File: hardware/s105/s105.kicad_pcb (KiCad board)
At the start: 2 copper layers, 20 parts, among them Q1 BC847C

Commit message: разместила схожие блоки
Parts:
- added C10: 2.2uF, Capacitor_SMD:C_0603_1608Metric, F.Cu at (219.5, 145.0)
- added C11: 2.2uF, Capacitor_SMD:C_0603_1608Metric, F.Cu at (228.2, 128.6)
- added C12: 1uF, Capacitor_SMD:C_0603_1608Metric, F.Cu at (208.7, 143.7)
- added C13: 10nF, Capacitor_SMD:C_0603_1608Metric, F.Cu at (269.1, 115.5)
- added C14: 100nF, Capacitor_SMD:C_0603_1608Metric, F.Cu at (221.0, 144.5)
- added C15: 100nF, Capacitor_SMD:C_0603_1608Metric, F.Cu at (225.8, 125.0)
- added C16: 100nF, Capacitor_SMD:C_0603_1608Metric, F.Cu at (203.9, 130.8)
- added C17: 100nF, Capacitor_SMD:C_0603_1608Metric, F.Cu at (208.9, 121.9)
- added C18: 100nF, Capacitor_SMD:C_0603_1608Metric, F.Cu at (208.7, 120.3)
- added C25: C0603, Capacitor_SMD:C_0603_1608Metric, F.Cu at (77.4, 181.7)
- added C26: C0603, Capacitor_SMD:C_0603_1608Metric, F.Cu at (77.4, 183.2)
- added C27: C0603, Capacitor_SMD:C_0603_1608Metric, F.Cu at (77.4, 178.7)
- added C28: NM, Capacitor_SMD:C_0603_1608Metric, F.Cu at (77.4, 180.2)
- added C29: C0603, Capacitor_SMD:C_0603_1608Metric, F.Cu at (77.4, 177.2)
- added C30: C0603, Capacitor_SMD:C_0603_1608Metric, F.Cu at (77.4, 175.7)
- added C31: C0603, Capacitor_SMD:C_0603_1608Metric, F.Cu at (77.4, 174.2)
- added C32: C0603, Capacitor_SMD:C_0603_1608Metric, F.Cu at (77.5, 187.4)
- added C33: C0603, Capacitor_SMD:C_0603_1608Metric, F.Cu at (77.5, 192.0)
- added C34: C0603, Capacitor_SMD:C_0603_1608Metric, F.Cu at (77.4, 207.0)
- added C35: C0603, Capacitor_SMD:C_0603_1608Metric, F.Cu at (77.5, 190.5)
- added C36: C0603, Capacitor_SMD:C_0603_1608Metric, F.Cu at (77.5, 188.9)
- added C37: C0603, Capacitor_SMD:C_0603_1608Metric, F.Cu at (77.4, 201.8)
- added C38: C0603, Capacitor_SMD:C_0603_1608Metric, F.Cu at (77.3, 205.1)
- added C39: C0603, Capacitor_SMD:C_0603_1608Metric, F.Cu at (77.3, 203.5)
- added C4: C0603, Capacitor_SMD:C_0603_1608Metric, F.Cu at (77.5, 184.7)
- added C40: C0603, Capacitor_SMD:C_0603_1608Metric, F.Cu at (77.5, 193.5)
- added C41: ~, Capacitor_SMD:C_0603_1608Metric, F.Cu at (99.4, 103.8)
- added C42: ~, Capacitor_SMD:C_0603_1608Metric, F.Cu at (101.3, 105.4)
- added C43: C_Small, Capacitor_SMD:C_1206_3216Metric, F.Cu at (74.9, 114.2)
- added C44: ~, Capacitor_SMD:C_0603_1608Metric, F.Cu at (142.7, 127.9)
- added C45: ~, Capacitor_SMD:C_0603_1608Metric, F.Cu at (142.9, 122.8)
- added C46: C_Small, Capacitor_SMD:C_1206_3216Metric, F.Cu at (77.8, 117.4)
- added C47: ~, Capacitor_SMD:C_0603_1608Metric, F.Cu at (139.1, 98.9)
- added C48: ~, Capacitor_SMD:C_0603_1608Metric, F.Cu at (142.4, 94.7)
- added C49: C_Small, Capacitor_SMD:C_1206_3216Metric, F.Cu at (73.9, 100.6)
- added C5: 10nF, Capacitor_SMD:C_0603_1608Metric, F.Cu at (264.8, 113.0)
- added C50: C0603, Capacitor_SMD:C_0603_1608Metric, F.Cu at (134.4, 236.0)
- added C51: C0805, Capacitor_SMD:C_0805_2012Metric, F.Cu at (196.2, 152.1)
- added C52: 100nF, Capacitor_SMD:C_0603_1608Metric, F.Cu at (200.4, 138.8)
- added C53: 100nF, Capacitor_SMD:C_0603_1608Metric, F.Cu at (197.4, 137.2)
- added C6: 18pF, Capacitor_SMD:C_0603_1608Metric, F.Cu at (199.3, 128.1)
- added C7: 18pF, Capacitor_SMD:C_0603_1608Metric, F.Cu at (199.3, 131.0)
- added C8: 1uF, Capacitor_SMD:C_0603_1608Metric, F.Cu at (200.0, 136.3)
- added C9: 100nF, Capacitor_SMD:C_0603_1608Metric, F.Cu at (227.8, 125.5)
- added D10: 1N4148W, Diode_SMD:D_SOD-123, F.Cu at (148.4, 98.5)
- added D11: BYG2OG, Diode_SMD:D_SMA, F.Cu at (151.9, 299.9)
- added D12: BYG2OG, Diode_SMD:D_SMA, F.Cu at (58.2, 297.1)
- added D13: BYG2OG, Diode_SMD:D_SMA, F.Cu at (216.6, 220.0)
- added D14: BYG2OG, Diode_SMD:D_SMA, F.Cu at (136.8, 260.6)
- added D15: 1N4148W, Diode_SMD:D_SOD-123, F.Cu at (125.7, 242.6)
- added D16: BYG2OG, Diode_SMD:D_SMA, F.Cu at (155.0, 237.6)
- added D17: BYG2OG, Diode_SMD:D_SMA, F.Cu at (108.3, 287.8)
- added D18: BYG2OG, Diode_SMD:D_SMA, F.Cu at (78.7, 269.3)
- added D19: BYG2OG, Diode_SMD:D_SMA, F.Cu at (208.0, 305.7)
- added D20: BYG2OG, Diode_SMD:D_SMA, F.Cu at (192.1, 199.4)
- added D7: BYG2OG, Diode_SMD:D_SMA, F.Cu at (123.2, 201.6)
- added D8: 1N4148W, Diode_SMD:D_SOD-123, F.Cu at (91.0, 103.9)
- added D9: 1N4148W, Diode_SMD:D_SOD-123, F.Cu at (147.6, 124.3)
- added J1: Conn_01x06, Connector_JST:JST_EH_B6B-EH-A_1x06_P2.50mm_Vertical, F.Cu at (230.6, 142.8)
- added P1: 368255-2, hellen121vag:368255-2, F.Cu at (126.1, 113.7)
- added Q10: BC847C, Package_TO_SOT_SMD:SOT-23, F.Cu at (220.9, 168.0)
- added Q11: BC847C, Package_TO_SOT_SMD:SOT-23, F.Cu at (127.3, 189.4)
- added Q12: BC847C, Package_TO_SOT_SMD:SOT-23, F.Cu at (156.0, 271.3)
- added Q13: BC847C, Package_TO_SOT_SMD:SOT-23, F.Cu at (176.3, 297.4)
- added Q14: BC847C, Package_TO_SOT_SMD:SOT-23, F.Cu at (81.3, 298.0)
- added Q15: BC847C, Package_TO_SOT_SMD:SOT-23, F.Cu at (220.2, 196.9)
- added Q16: BC847C, Package_TO_SOT_SMD:SOT-23, F.Cu at (118.0, 240.3)
- added Q17: ., Package_TO_SOT_SMD:SOT-23, F.Cu at (127.7, 236.6)
- added Q18: BC847C, Package_TO_SOT_SMD:SOT-23, F.Cu at (180.7, 226.6)
- added Q19: ., Package_TO_SOT_SMD:SOT-23, F.Cu at (118.0, 236.8)
- added Q2: BC847C, Package_TO_SOT_SMD:SOT-23, F.Cu at (146.4, 209.7)
- added Q20: BC847C, Package_TO_SOT_SMD:SOT-23, F.Cu at (130.3, 296.8)
- added Q21: BC847C, Package_TO_SOT_SMD:SOT-23, F.Cu at (103.6, 264.6)
- added Q22: BC847C, Package_TO_SOT_SMD:SOT-23, F.Cu at (219.6, 284.9)
- added Q23: BC847C, Package_TO_SOT_SMD:SOT-23, F.Cu at (177.6, 216.8)
- added Q24: ., Package_TO_SOT_SMD:SOT-23, F.Cu at (217.8, 150.6)
- added Q25: ., Package_TO_SOT_SMD:SOT-23, F.Cu at (214.1, 150.7)
- added Q26: ., Package_TO_SOT_SMD:SOT-23, F.Cu at (210.4, 150.6)
- added Q27: ., Package_TO_SOT_SMD:SOT-23, F.Cu at (221.3, 150.6)
- added Q28: ., Package_TO_SOT_SMD:SOT-23, F.Cu at (195.3, 148.3)
- added Q29: ., Package_TO_SOT_SMD:SOT-23, F.Cu at (201.1, 119.1)
- added Q3: BC847C, Package_TO_SOT_SMD:SOT-23, F.Cu at (92.0, 211.5)
- added Q30: ., Package_TO_SOT_SMD:SOT-23, F.Cu at (198.6, 123.1)
- added Q31: ., Package_TO_SOT_SMD:SOT-23, F.Cu at (214.0, 115.4)
- added Q32: ., Package_TO_SOT_SMD:SOT-23, F.Cu at (216.6, 109.3)
- added Q33: ., Package_TO_SOT_SMD:SOT-23, F.Cu at (221.0, 118.8)
- added Q4: BC847C, Package_TO_SOT_SMD:SOT-23, F.Cu at (210.5, 260.0)
- added Q5: ., Package_TO_SOT_SMD:SOT-23, F.Cu at (216.4, 253.8)
- added Q6: ., Package_TO_SOT_SMD:SOT-23, F.Cu at (221.6, 252.6)
- added Q7: BC847C, Package_TO_SOT_SMD:SOT-23, F.Cu at (105.8, 224.8)
- added Q8: BC847C, Package_TO_SOT_SMD:SOT-23, F.Cu at (201.7, 225.9)
- added Q9: BC847C, Package_TO_SOT_SMD:SOT-23, F.Cu at (193.6, 177.4)
- added R100: 1R, Resistor_SMD:R_1206_3216Metric, F.Cu at (210.2, 173.9)
- added R101: 1R, Resistor_SMD:R_1206_3216Metric, F.Cu at (210.2, 177.7)
- added R102: 82K, Resistor_SMD:R_0805_2012Metric, F.Cu at (211.1, 188.5)
- added R103: 51K, Resistor_SMD:R_0603_1608Metric, F.Cu at (207.7, 187.4)
- added R104: 3K, Resistor_SMD:R_0603_1608Metric, F.Cu at (128.0, 182.7)
- added R105: 3K, Resistor_SMD:R_0603_1608Metric, F.Cu at (128.1, 185.2)
- added R106: 360R, Resistor_SMD:R_0603_1608Metric, F.Cu at (128.5, 194.6)
- added R107: 1R, Resistor_SMD:R_1206_3216Metric, F.Cu at (139.2, 196.2)
- added R108: 1R, Resistor_SMD:R_1206_3216Metric, F.Cu at (132.5, 196.3)
- added R109: 1R, Resistor_SMD:R_1206_3216Metric, F.Cu at (135.9, 196.2)
- added R110: 82K, Resistor_SMD:R_0805_2012Metric, F.Cu at (145.6, 195.6)
- added R111: 51K, Resistor_SMD:R_0603_1608Metric, F.Cu at (144.7, 198.5)
- added R112: 3K, Resistor_SMD:R_0603_1608Metric, F.Cu at (155.2, 267.5)
- added R113: 3K, Resistor_SMD:R_0603_1608Metric, F.Cu at (160.1, 270.2)
- added R114: 360R, Resistor_SMD:R_0603_1608Metric, F.Cu at (157.5, 278.6)
- added R115: 1R, Resistor_SMD:R_1206_3216Metric, F.Cu at (168.2, 280.4)
- added R116: 1R, Resistor_SMD:R_1206_3216Metric, F.Cu at (161.0, 280.1)
- added R117: 1R, Resistor_SMD:R_1206_3216Metric, F.Cu at (164.6, 280.3)
- added R118: 82K, Resistor_SMD:R_0805_2012Metric, F.Cu at (173.2, 278.8)
- added R119: 51K, Resistor_SMD:R_0603_1608Metric, F.Cu at (172.3, 281.7)
- added R120: 3K, Resistor_SMD:R_0603_1608Metric, F.Cu at (177.2, 301.4)
- added R121: 3K, Resistor_SMD:R_0603_1608Metric, F.Cu at (171.8, 298.7)
- added R122: 360R, Resistor_SMD:R_0603_1608Metric, F.Cu at (176.0, 290.8)
- added R123: 1R, Resistor_SMD:R_1206_3216Metric, F.Cu at (163.9, 290.0)
- added R124: 1R, Resistor_SMD:R_1206_3216Metric, F.Cu at (171.2, 290.2)
- added R125: 1R, Resistor_SMD:R_1206_3216Metric, F.Cu at (167.6, 290.0)
- added R126: 82K, Resistor_SMD:R_0805_2012Metric, F.Cu at (158.7, 290.8)
- added R127: 51K, Resistor_SMD:R_0603_1608Metric, F.Cu at (159.5, 287.6)
- added R128: 3K, Resistor_SMD:R_0603_1608Metric, F.Cu at (82.0, 302.1)
- added R129: 3K, Resistor_SMD:R_0603_1608Metric, F.Cu at (76.7, 299.6)
- added R130: 360R, Resistor_SMD:R_0603_1608Metric, F.Cu at (80.5, 290.8)
- added R131: 1R, Resistor_SMD:R_1206_3216Metric, F.Cu at (68.1, 290.4)
- added R132: 1R, Resistor_SMD:R_1206_3216Metric, F.Cu at (74.9, 290.3)
- added R133: 1R, Resistor_SMD:R_1206_3216Metric, F.Cu at (71.4, 290.3)
- added R134: 82K, Resistor_SMD:R_0805_2012Metric, F.Cu at (63.6, 291.5)
- added R135: 51K, Resistor_SMD:R_0603_1608Metric, F.Cu at (64.5, 288.4)
- added R136: 3K, Resistor_SMD:R_0603_1608Metric, F.Cu at (224.2, 196.6)
- added R137: 3K, Resistor_SMD:R_0603_1608Metric, F.Cu at (221.0, 201.6)
- added R138: 360R, Resistor_SMD:R_0603_1608Metric, F.Cu at (215.0, 196.4)
- added R139: 1R, Resistor_SMD:R_1206_3216Metric, F.Cu at (211.3, 207.9)
- added R14: 10K, Resistor_SMD:R_0603_1608Metric, F.Cu at (268.8, 111.5)
- added R140: 1R, Resistor_SMD:R_1206_3216Metric, F.Cu at (211.8, 201.7)
- added R141: 1R, Resistor_SMD:R_1206_3216Metric, F.Cu at (211.4, 204.6)
- added R142: 82K, Resistor_SMD:R_0805_2012Metric, F.Cu at (212.3, 214.3)
- added R143: 51K, Resistor_SMD:R_0603_1608Metric, F.Cu at (208.7, 215.2)
- added R144: 3K, Resistor_SMD:R_0603_1608Metric, F.Cu at (119.1, 245.3)
- added R145: 3K, Resistor_SMD:R_0603_1608Metric, F.Cu at (121.4, 245.1)
- added R146: 360R, Resistor_SMD:R_0603_1608Metric, F.Cu at (113.7, 255.3)
- added R147: 1R, Resistor_SMD:R_1206_3216Metric, F.Cu at (124.4, 260.1)
- added R148: 1R, Resistor_SMD:R_1206_3216Metric, F.Cu at (117.8, 260.0)
- added R149: 1R, Resistor_SMD:R_1206_3216Metric, F.Cu at (121.3, 260.1)
- added R15: 10K, Resistor_SMD:R_0603_1608Metric, F.Cu at (265.1, 115.5)
- added R150: 82K, Resistor_SMD:R_0805_2012Metric, F.Cu at (139.5, 253.6)
- added R151: 51K, Resistor_SMD:R_0603_1608Metric, F.Cu at (139.5, 251.2)
- added R152: 6.8k, Resistor_SMD:R_0603_1608Metric, F.Cu at (134.4, 233.8)
- added R153: 100, Resistor_SMD:R_0603_1608Metric, F.Cu at (130.6, 233.8)
- added R154: 68k, Resistor_SMD:R_0603_1608Metric, F.Cu at (131.9, 236.8)
- added R155: 4.7k, Resistor_SMD:R_1206_3216Metric, F.Cu at (133.4, 239.9)
- added R156: 4.7k, Resistor_SMD:R_1206_3216Metric, F.Cu at (133.4, 242.3)
- added R157: 10k, Resistor_SMD:R_0805_2012Metric, F.Cu at (128.7, 241.9)
- added R158: 100, Resistor_SMD:R_0603_1608Metric, F.Cu at (121.5, 235.9)
- added R159: 3K, Resistor_SMD:R_0603_1608Metric, F.Cu at (176.3, 234.9)
- added R160: 3K, Resistor_SMD:R_0603_1608Metric, F.Cu at (179.6, 235.9)
- added R161: 360R, Resistor_SMD:R_0603_1608Metric, F.Cu at (181.1, 224.0)
- added R162: 1R, Resistor_SMD:R_1206_3216Metric, F.Cu at (173.9, 222.4)
- added R163: 1R, Resistor_SMD:R_1206_3216Metric, F.Cu at (174.0, 227.0)
- added R164: 1R, Resistor_SMD:R_1206_3216Metric, F.Cu at (174.0, 224.7)
- added R165: 82K, Resistor_SMD:R_0805_2012Metric, F.Cu at (161.6, 227.1)
- added R166: 51K, Resistor_SMD:R_0603_1608Metric, F.Cu at (162.3, 223.6)
- added R167: 3K, Resistor_SMD:R_0603_1608Metric, F.Cu at (131.0, 300.5)
- added R168: 3K, Resistor_SMD:R_0603_1608Metric, F.Cu at (126.2, 298.0)
- added R169: 360R, Resistor_SMD:R_0603_1608Metric, F.Cu at (129.5, 291.4)
- added R170: 1R, Resistor_SMD:R_1206_3216Metric, F.Cu at (118.3, 289.3)
- added R171: 1R, Resistor_SMD:R_1206_3216Metric, F.Cu at (125.4, 289.4)
- added R172: 1R, Resistor_SMD:R_1206_3216Metric, F.Cu at (121.7, 289.3)
- added R173: 82K, Resistor_SMD:R_0805_2012Metric, F.Cu at (113.2, 290.1)
- added R174: 51K, Resistor_SMD:R_0603_1608Metric, F.Cu at (114.1, 286.6)
- added R175: 3K, Resistor_SMD:R_0603_1608Metric, F.Cu at (104.0, 268.5)
- added R176: 3K, Resistor_SMD:R_0603_1608Metric, F.Cu at (99.8, 266.3)
- added R177: 360R, Resistor_SMD:R_0603_1608Metric, F.Cu at (103.5, 258.8)
- added R178: 1R, Resistor_SMD:R_1206_3216Metric, F.Cu at (92.6, 257.2)
- added R179: 1R, Resistor_SMD:R_1206_3216Metric, F.Cu at (99.0, 257.0)
- added R180: 1R, Resistor_SMD:R_1206_3216Metric, F.Cu at (95.8, 257.2)
- added R181: 82K, Resistor_SMD:R_0805_2012Metric, F.Cu at (86.6, 257.2)
- added R182: 51K, Resistor_SMD:R_0603_1608Metric, F.Cu at (87.5, 254.1)
- added R183: 3K, Resistor_SMD:R_0603_1608Metric, F.Cu at (225.4, 284.9)
- added R184: 3K, Resistor_SMD:R_0603_1608Metric, F.Cu at (225.4, 289.3)
- added R185: 360R, Resistor_SMD:R_0603_1608Metric, F.Cu at (214.9, 281.0)
- added R186: 1R, Resistor_SMD:R_1206_3216Metric, F.Cu at (209.7, 296.3)
- added R187: 1R, Resistor_SMD:R_1206_3216Metric, F.Cu at (209.9, 289.1)
- added R188: 1R, Resistor_SMD:R_1206_3216Metric, F.Cu at (209.9, 292.6)
- added R189: 82K, Resistor_SMD:R_0805_2012Metric, F.Cu at (210.2, 300.8)
- added R19: 3K, Resistor_SMD:R_0603_1608Metric, F.Cu at (147.2, 213.6)
- added R190: 51K, Resistor_SMD:R_0603_1608Metric, F.Cu at (206.7, 299.9)
- added R191: 3K, Resistor_SMD:R_0603_1608Metric, F.Cu at (175.2, 205.1)
- added R192: 3K, Resistor_SMD:R_0603_1608Metric, F.Cu at (180.1, 207.7)
- added R193: 360R, Resistor_SMD:R_0603_1608Metric, F.Cu at (179.1, 213.6)
- added R194: 1R, Resistor_SMD:R_1206_3216Metric, F.Cu at (190.3, 217.2)
- added R195: 1R, Resistor_SMD:R_1206_3216Metric, F.Cu at (182.6, 216.8)
- added R196: 1R, Resistor_SMD:R_1206_3216Metric, F.Cu at (186.8, 217.0)
- added R197: 82K, Resistor_SMD:R_0805_2012Metric, F.Cu at (193.8, 216.2)
- added R198: 51K, Resistor_SMD:R_0603_1608Metric, F.Cu at (192.8, 219.3)
- added R199: 6.8k, Resistor_SMD:R_0603_1608Metric, F.Cu at (198.9, 152.0)
- added R20: 3K, Resistor_SMD:R_0603_1608Metric, F.Cu at (142.3, 210.8)
- added R200: 68k, Resistor_SMD:R_0603_1608Metric, F.Cu at (200.9, 151.9)
- added R201: R0603, Resistor_SMD:R_0603_1608Metric, F.Cu at (194.4, 133.6)
- added R202: 300, Resistor_SMD:R_0603_1608Metric, F.Cu at (201.0, 131.0)
- added R21: 360R, Resistor_SMD:R_0603_1608Metric, F.Cu at (144.3, 204.2)
- added R22: 1R, Resistor_SMD:R_1206_3216Metric, F.Cu at (133.5, 202.1)
- added R23: 1R, Resistor_SMD:R_1206_3216Metric, F.Cu at (140.5, 202.1)
- added R24: 1R, Resistor_SMD:R_1206_3216Metric, F.Cu at (137.0, 202.2)
- added R25: 82K, Resistor_SMD:R_0805_2012Metric, F.Cu at (127.9, 203.4)
- added R26: 51K, Resistor_SMD:R_0603_1608Metric, F.Cu at (129.4, 200.4)
- added R27: 3K, Resistor_SMD:R_0603_1608Metric, F.Cu at (86.9, 209.9)
- added R28: 3K, Resistor_SMD:R_0603_1608Metric, F.Cu at (90.9, 208.3)
- added R29: 360R, Resistor_SMD:R_0603_1608Metric, F.Cu at (99.4, 209.3)
- added R30: 1R, Resistor_SMD:R_1206_3216Metric, F.Cu at (101.2, 205.4)
- added R31: 1R, Resistor_SMD:R_1206_3216Metric, F.Cu at (101.2, 202.8)
- added R32: 1R, Resistor_SMD:R_1206_3216Metric, F.Cu at (101.2, 200.0)
- added R33: 82K, Resistor_SMD:R_0805_2012Metric, F.Cu at (99.7, 194.6)
- added R34: 51K, Resistor_SMD:R_0603_1608Metric, F.Cu at (103.7, 195.7)
- added R35: 3K, Resistor_SMD:R_0603_1608Metric, F.Cu at (219.2, 259.8)
- added R36: 3K, Resistor_SMD:R_0603_1608Metric, F.Cu at (221.6, 260.5)
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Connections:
- net /IGN driver/FB renamed /PC3
- net /IGN driver/OUT renamed /IGN_1
- net /OD 2A/FB renamed /PA15
- net /OD 2A/IN renamed /PE6
- net /OD 2A/OUT renamed /INJ_1
- net GNDPWR renamed GND
- D1 pad 1: +5V -> VD
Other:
- board outline added: 189.1 x 227.2 mm
- board text added: "+2 по 100 ОМ"
- board text added: "1"
- board text added: "10"
- board text added: "11"
- board text added: "12"
- board text added: "13"
- board text added: "14"
- board text added: "15"
- board text added: "16"
- board text added: "17"
- board text added: "18"
- board text added: "19"
- board text added: "2"
- board text added: "20"
- board text added: "21"
- board text added: "22"
- board text added: "23"
- board text added: "24"
- board text added: "25"
- board text added: "26"
- board text added: "27"
- board text added: "28"
- board text added: "29"
- board text added: "3"
- board text added: "30"
- board text added: "31"
- board text added: "32"
- board text added: "33"
- board text added: "34"
- board text added: "35"
- board text added: "36"
- board text added: "37"
- board text added: "38"
- board text added: "39"
- board text added: "4"
- board text added: "40"
- board text added: "41"
- board text added: "42"
- board text added: "43"
- board text added: "44"
- board text added: "45"
- board text added: "46"
- board text added: "47"
- board text added: "48"
- board text added: "49"
- board text added: "5"
- board text added: "50"
- board text added: "51"
- board text added: "52"
- board text added: "53"
- board text added: "54"
- board text added: "55"
- board text added: "56"
- board text added: "57"
- board text added: "58"
- board text added: "59"
- board text added: "6"
- board text added: "60"
- board text added: "61"
- board text added: "62"
- board text added: "63"
- board text added: "64"
- board text added: "65"
- board text added: "66"
- board text added: "67"
- board text added: "68"
- board text added: "69"
- board text added: "7"
- board text added: "70"
- board text added: "71"
- board text added: "72"
- board text added: "73"
- board text added: "74"
- board text added: "75"
- board text added: "76"
- board text added: "77"
- board text added: "78"
- board text added: "79"
- board text added: "8"
- board text added: "80"
- board text added: "81"
- board text added: "9"

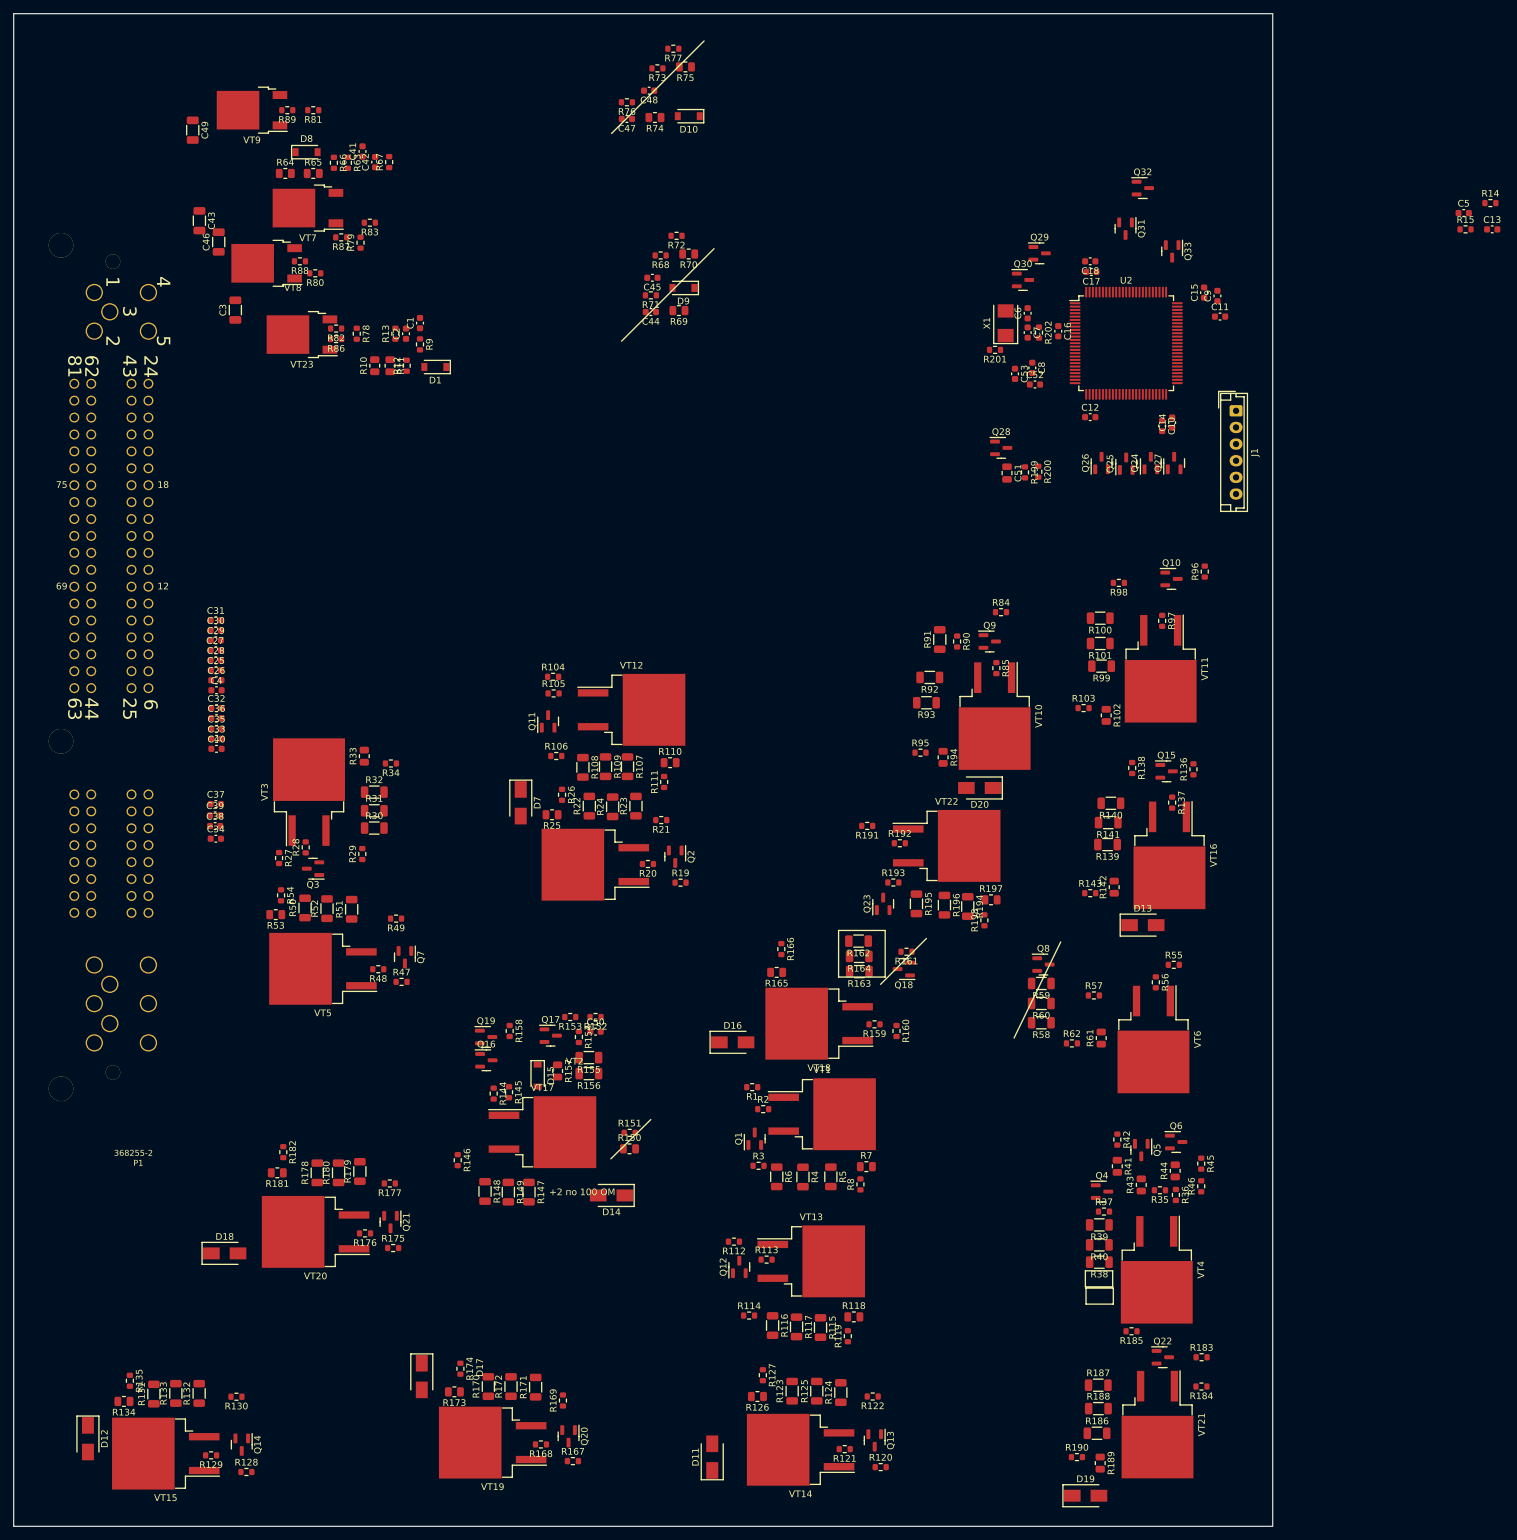
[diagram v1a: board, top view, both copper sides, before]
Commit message: вписала в габариты платы, продолжила опознание
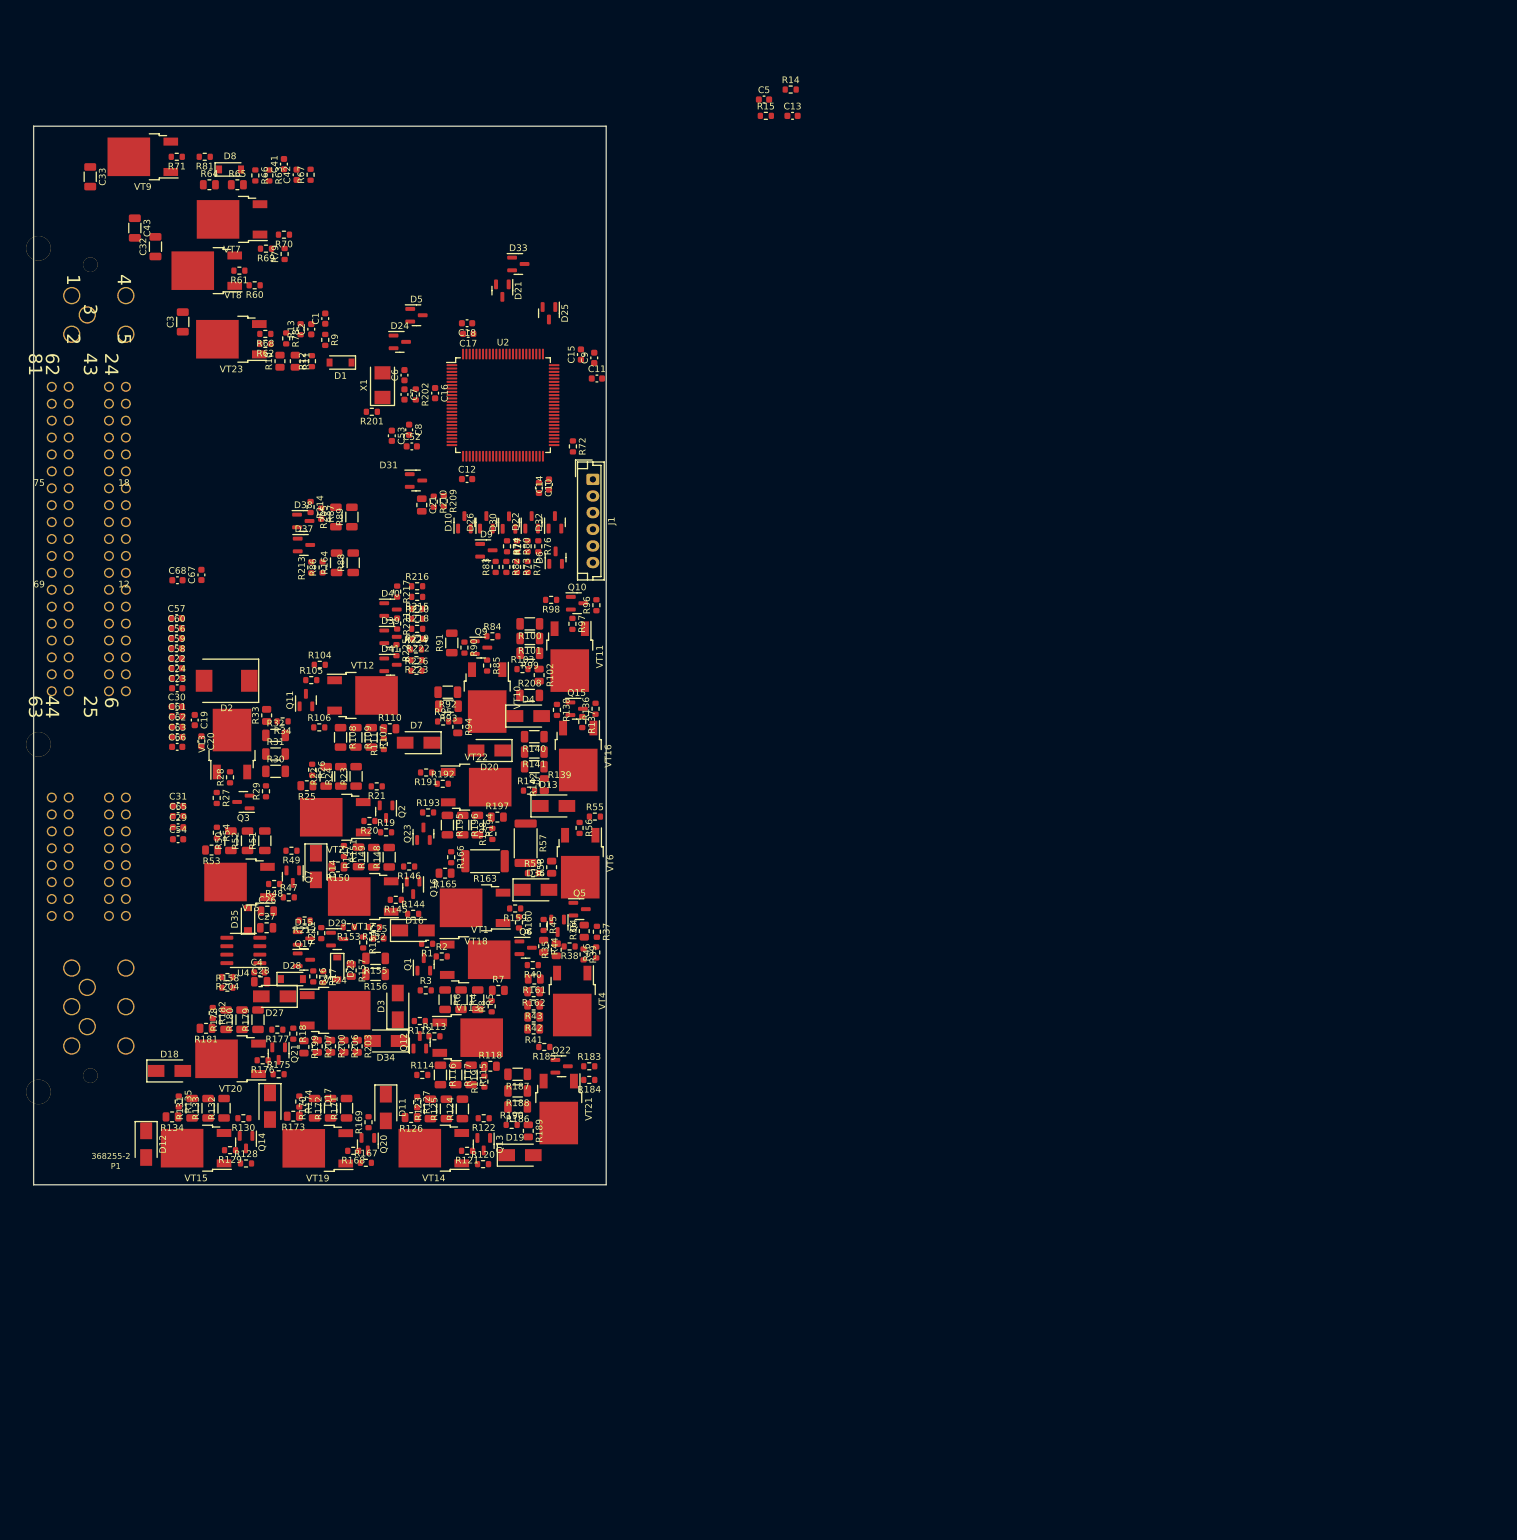
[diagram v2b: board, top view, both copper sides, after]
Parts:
- removed C34, C35, C36, C37, C38, C39, C40, C50: C0603, Capacitor_SMD:C_0603_1608Metric
- removed C44, C45, C47, C48: ~, Capacitor_SMD:C_0603_1608Metric
- removed C46, C49: C_Small, Capacitor_SMD:C_1206_3216Metric
- removed C51: C0805, Capacitor_SMD:C_0805_2012Metric
- removed Q18, Q8: BC847C, Package_TO_SOT_SMD:SOT-23
- removed Q19, Q24, Q25, Q26, Q27, Q28, Q29, Q30, Q31, Q32, Q33: ., Package_TO_SOT_SMD:SOT-23
- added C19: C0603, Capacitor_SMD:C_0603_1608Metric, F.Cu at (74.2, 189.2)
- added C20: C0603, Capacitor_SMD:C_0603_1608Metric, F.Cu at (75.2, 192.4)
- added C21: C0805, Capacitor_SMD:C_0805_2012Metric, F.Cu at (108.3, 156.9)
- added C22: C0603, Capacitor_SMD:C_0603_1608Metric, F.Cu at (71.5, 181.4)
- added C23: C0603, Capacitor_SMD:C_0603_1608Metric, F.Cu at (71.6, 184.4)
- added C24: C0603, Capacitor_SMD:C_0603_1608Metric, F.Cu at (71.5, 182.9)
- added C54: C0603, Capacitor_SMD:C_0603_1608Metric, F.Cu at (71.7, 207.1)
- added C56: C0603, Capacitor_SMD:C_0603_1608Metric, F.Cu at (71.5, 176.9)
- added C57: C0603, Capacitor_SMD:C_0603_1608Metric, F.Cu at (71.5, 173.9)
- added C58: C0603, Capacitor_SMD:C_0603_1608Metric, F.Cu at (71.5, 179.9)
- added C59: C0603, Capacitor_SMD:C_0603_1608Metric, F.Cu at (71.5, 178.4)
- added C60: C0603, Capacitor_SMD:C_0603_1608Metric, F.Cu at (71.5, 175.4)
- added C61: C0603, Capacitor_SMD:C_0603_1608Metric, F.Cu at (71.6, 188.6)
- added C62: C0603, Capacitor_SMD:C_0603_1608Metric, F.Cu at (71.6, 190.2)
- added C63: C0603, Capacitor_SMD:C_0603_1608Metric, F.Cu at (71.6, 191.7)
- added C65: C0603, Capacitor_SMD:C_0603_1608Metric, F.Cu at (71.7, 203.6)
- added C66: C0603, Capacitor_SMD:C_0603_1608Metric, F.Cu at (71.6, 193.2)
- added C67: C0603, Capacitor_SMD:C_0603_1608Metric, F.Cu at (75.2, 167.4)
- added C68: C0603, Capacitor_SMD:C_0603_1608Metric, F.Cu at (71.6, 168.2)
- added D2: ., Diode_SMD:D_SMC, F.Cu at (79.0, 183.3)
- added D21: BAV99, Package_TO_SOT_SMD:SOT-23, F.Cu at (120.4, 124.7)
- added D22: BAV99, Package_TO_SOT_SMD:SOT-23, F.Cu at (124.8, 159.5)
- added D23: 1N4148W, Diode_SMD:D_SOD-123, F.Cu at (95.6, 226.5)
- added D24: BAV99, Package_TO_SOT_SMD:SOT-23, F.Cu at (105.0, 132.4)
- added D25: BAV99, Package_TO_SOT_SMD:SOT-23, F.Cu at (127.4, 128.1)
- added D26: BAV99, Package_TO_SOT_SMD:SOT-23, F.Cu at (118.0, 159.5)
- added D27: ., Diode_SMD:D_SMA, F.Cu at (86.2, 230.7)
- added D28: 1N4148W, Diode_SMD:D_SOD-123, F.Cu at (88.8, 228.1)
- added D29: BAV99, Package_TO_SOT_SMD:SOT-23, F.Cu at (95.6, 222.1)
- added D3: NM, Diode_SMD:D_SMA, F.Cu at (104.7, 232.2)
- added D30: BAV99, Package_TO_SOT_SMD:SOT-23, F.Cu at (121.4, 159.5)
- added D31: BAV99, Package_TO_SOT_SMD:SOT-23, F.Cu at (107.4, 153.2)
- added D32: BAV99, Package_TO_SOT_SMD:SOT-23, F.Cu at (128.3, 159.5)
- added D33: BAV99, Package_TO_SOT_SMD:SOT-23, F.Cu at (122.8, 120.7)
- added D34: ., Diode_SMD:D_SMA, F.Cu at (102.9, 237.4)
- added D35: ., Diode_SMD:D_SOD-123, F.Cu at (82.2, 219.1)
- added D36: BYG2OG, Diode_SMD:D_SMA, F.Cu at (125.4, 214.7)
- added D37: BAV99, Package_TO_SOT_SMD:SOT-23, F.Cu at (90.6, 162.9)
- added D38: BAV99, Package_TO_SOT_SMD:SOT-23, F.Cu at (90.5, 159.3)
- added D39: BAV99, Package_TO_SOT_SMD:SOT-23, F.Cu at (103.6, 176.7)
- added D4: BYG2OG, Diode_SMD:D_SMA, F.Cu at (124.3, 188.6)
- added D40: BAV99, Package_TO_SOT_SMD:SOT-23, F.Cu at (103.6, 172.6)
- added D41: BAV99, Package_TO_SOT_SMD:SOT-23, F.Cu at (103.6, 180.9)
- added D5: BAV99, Package_TO_SOT_SMD:SOT-23, F.Cu at (107.5, 128.4)
- added D6: BAV99, Package_TO_SOT_SMD:SOT-23, F.Cu at (128.4, 164.8)
- added R16: 3K, Resistor_SMD:R_0603_1608Metric, F.Cu at (92.0, 227.7)
- added R17: 3K, Resistor_SMD:R_0603_1608Metric, F.Cu at (93.5, 227.8)
- added R18: 360R, Resistor_SMD:R_0603_1608Metric, F.Cu at (89.0, 236.3)
- added R203: 10R, Resistor_SMD:R_0805_2012Metric, F.Cu at (98.6, 238.2)
- added R204: 1K, Resistor_SMD:R_0603_1608Metric, F.Cu at (79.1, 227.8)
- added R205: 3k, Resistor_SMD:R_1206_3216Metric, F.Cu at (95.4, 158.7)
- added R206: 10R, Resistor_SMD:R_0805_2012Metric, F.Cu at (96.6, 238.2)
- added R207: 10R, Resistor_SMD:R_0805_2012Metric, F.Cu at (92.6, 238.2)
- added R208: 4.7k, Resistor_SMD:R_1206_3216Metric, F.Cu at (124.5, 185.5)
- added R209: 68k, Resistor_SMD:R_0603_1608Metric, F.Cu at (111.6, 156.3)
- added R210: 6.8k, Resistor_SMD:R_0603_1608Metric, F.Cu at (110.1, 156.4)
- added R211: 10k, Resistor_SMD:R_0603_1608Metric, F.Cu at (93.2, 221.2)
- added R212: NM, Resistor_SMD:R_0603_1608Metric, F.Cu at (90.7, 219.3)
- added R213: 22k, Resistor_SMD:R_0603_1608Metric, F.Cu at (91.7, 166.3)
- added R214: 22k, Resistor_SMD:R_0603_1608Metric, F.Cu at (91.6, 157.2)
- added R215: 10k, Resistor_SMD:R_0603_1608Metric, F.Cu at (107.6, 170.7)
- added R216: NM, Resistor_SMD:R_0603_1608Metric, F.Cu at (107.6, 169.1)
- added R217: 22k, Resistor_SMD:R_0603_1608Metric, F.Cu at (104.6, 169.9)
- added R218: 60k, Resistor_SMD:R_0603_1608Metric, F.Cu at (107.6, 172.5)
- added R219: 10k, Resistor_SMD:R_0603_1608Metric, F.Cu at (107.6, 175.5)
- added R220: NM, Resistor_SMD:R_0603_1608Metric, F.Cu at (107.6, 174.0)
- added R221: 22k, Resistor_SMD:R_0603_1608Metric, F.Cu at (104.6, 174.7)
- added R222: 60k, Resistor_SMD:R_0603_1608Metric, F.Cu at (107.7, 177.0)
- added R223: NM, Resistor_SMD:R_0603_1608Metric, F.Cu at (107.5, 180.2)
- added R224: NM, Resistor_SMD:R_0603_1608Metric, F.Cu at (107.4, 178.6)
- added R225: NM, Resistor_SMD:R_0603_1608Metric, F.Cu at (104.5, 178.7)
- added R226: NM, Resistor_SMD:R_0603_1608Metric, F.Cu at (107.5, 181.8)
- added U4: case only, Package_SO:SOIC-8_3.9x4.9mm_P1.27mm, F.Cu at (81.5, 223.8)
- added VT24: IRLR3110Z, Package_TO_SOT_SMD:TO-252-2, F.Cu at (95.3, 232.8)
- C26, C27: value C0603 -> C0805; footprint Capacitor_SMD:C_0603_1608Metric -> Capacitor_SMD:C_0805_2012Metric
- C28: value NM -> C0805; footprint Capacitor_SMD:C_0603_1608Metric -> Capacitor_SMD:C_0805_2012Metric
- C32, C33: value C0603 -> C_Small; footprint Capacitor_SMD:C_0603_1608Metric -> Capacitor_SMD:C_1206_3216Metric
- D10, D15, D9: value 1N4148W -> BAV99; footprint Diode_SMD:D_SOD-123 -> Package_TO_SOT_SMD:SOT-23
- Q17, Q6: value . -> BC847C
- Q4: value BC847C -> .
- R153: value 100 -> 1k
- R158: value 100 -> 47k
- R161: value 360R -> 10R; footprint Resistor_SMD:R_0603_1608Metric -> Resistor_SMD:R_0805_2012Metric
- R162: value 1R -> 10R; footprint Resistor_SMD:R_1206_3216Metric -> Resistor_SMD:R_0805_2012Metric
- R163: value 1R -> 50k?; footprint Resistor_SMD:R_1206_3216Metric -> Resistor_SMD:R_2512_6332Metric
- R164: value 1R -> 3k
- R199: value 6.8k -> 10R; footprint Resistor_SMD:R_0603_1608Metric -> Resistor_SMD:R_0805_2012Metric
- R200: value 68k -> 10R; footprint Resistor_SMD:R_0603_1608Metric -> Resistor_SMD:R_0805_2012Metric
- R35: value 3K -> 6.8k; footprint Resistor_SMD:R_0603_1608Metric -> Resistor_SMD:R_0805_2012Metric
- R36: value 3K -> 2.2k; footprint Resistor_SMD:R_0603_1608Metric -> Resistor_SMD:R_0805_2012Metric
- R37: value 360R -> 3K
- R38: value 1R -> 18K; footprint Resistor_SMD:R_1206_3216Metric -> Resistor_SMD:R_0603_1608Metric
- R39: value 1R -> 3K; footprint Resistor_SMD:R_1206_3216Metric -> Resistor_SMD:R_0603_1608Metric
- R40: value 1R -> 360R; footprint Resistor_SMD:R_1206_3216Metric -> Resistor_SMD:R_0603_1608Metric
- R41: value 82K -> 10R
- R42: value 51K -> 10R; footprint Resistor_SMD:R_0603_1608Metric -> Resistor_SMD:R_0805_2012Metric
- R43: value 6.8k -> 10R
- R44: value 2.2k -> 82K
- R45: value 3K -> 51K
- R57: value 360R -> 50k?; footprint Resistor_SMD:R_0603_1608Metric -> Resistor_SMD:R_2512_6332Metric
- R58: value 1R -> 82K; footprint Resistor_SMD:R_1206_3216Metric -> Resistor_SMD:R_0805_2012Metric
- R59: value 1R -> 51K; footprint Resistor_SMD:R_1206_3216Metric -> Resistor_SMD:R_0603_1608Metric
- R60: value 1R -> 100; footprint Resistor_SMD:R_1206_3216Metric -> Resistor_SMD:R_0603_1608Metric
- R61: value 82K -> 100; footprint Resistor_SMD:R_0805_2012Metric -> Resistor_SMD:R_0603_1608Metric
- R62: value 51K -> 100
- R68, R73: value 8K2 -> NM
- R69: value 10K -> 100; footprint Resistor_SMD:R_0805_2012Metric -> Resistor_SMD:R_0603_1608Metric
- R70, R74, R75: value 10K -> NM; footprint Resistor_SMD:R_0805_2012Metric -> Resistor_SMD:R_0603_1608Metric
- R71: value 3K -> 100
- R72: value 6K8 -> R0603
- R76: value 3K -> 22K
- R77: value 6K8 -> 510K
- R80: value 100 -> 1K
- R86, R87: value 100 -> 22k
- R88, R89: value 100 -> 3k; footprint Resistor_SMD:R_0603_1608Metric -> Resistor_SMD:R_1206_3216Metric
- VT1, VT10, VT11, VT12, VT13, VT14, VT15, VT16, VT17, VT18, VT19, VT2, VT20, VT21, VT22, VT3, VT4, VT5, VT6: footprint Package_TO_SOT_SMD:TO-263-2 -> Package_TO_SOT_SMD:TO-252-2
- moved R61 173.3 mm to (80.9, 121.7), turned to 180 degrees
- moved R62 160.4 mm to (84.8, 132.7), turned to 180 degrees
- moved R60 160.0 mm to (83.2, 123.9)
- moved R199 138.5 mm to (90.6, 238.3)
- moved R200 136.9 mm to (94.6, 238.2)
- moved C5 106.5 mm to (159.7, 96.0)
- moved R14 106.5 mm to (163.7, 94.5)
- moved R15 106.5 mm to (160.0, 98.5)
- moved C13 106.5 mm to (164.0, 98.5)
- moved R45 105.1 mm to (126.6, 220.0)
- moved R184 102.8 mm to (133.4, 243.2)
- moved Q6 102.0 mm to (123.9, 223.4)
- moved R183 101.8 mm to (133.4, 241.2)
- moved VT21 101.7 mm to (128.9, 247.6)
- moved R44 100.7 mm to (126.6, 223.2), turned to -90 degrees
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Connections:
- net /!!\ renamed /PE3
- net /MCU/PA0 renamed /PA0
- net /MCU/PA1 renamed /PA1
- net Net-(NT1-Pad1) renamed /MCU/PA9
- C25 pad 1: /INJ_1 -> Net-(C25-Pad1)
- C26 pad 1: /INJ_3 -> +12V
- C27 pad 1: /Idle_valve_close -> Net-(C27-Pad1)
- C28 pad 1: /TACH -> +5V
- C29 pad 1: /Unk_Out_1 -> /AFR_1_Heater
- C30 pad 1: /Idle_valve_open -> /INJ_7
- C31 pad 1: /ECO/CLT_Out -> /INJ_6/AFR_2_Heater
- C32 pad 1: /INJ_7 -> /IGN_3
- C33 pad 1: /Absorber -> /IGN_4
- C4 pad 1: /INJ_2 -> +5V
- D1 pad 1: VD -> +12V
- D10 pad 1: /IGN driver3/5V -> GND
- D10 pad 2: Net-(D10-Pad2) -> +3.3V
- D11 pad 1: VD -> +12V
- D12 pad 1: VD -> +12V
- D13 pad 1: VD -> +12V
- D15 pad 1: Net-(D15-Pad1) -> GND
- D15 pad 2: /!!! -> unconnected-(D15-Pad2)
- D16 pad 1: VD -> +12V
- D17 pad 1: VD -> +12V
- D18 pad 1: VD -> +12V
- D19 pad 1: VD -> +12V
- D20 pad 1: VD -> +12V
- D7 pad 1: VD -> +12V
- D7 pad 2: /INJ_2 -> /TACH
- D8 pad 1: VD -> +12V
- D9 pad 1: /IGN driver2/5V -> GND
- D9 pad 2: Net-(D9-Pad2) -> +3.3V
- P1 pad 44: /+12_Sens -> +12V
- P1 pad 45: unconnected-(P1-Pad45) -> +12V
- Q16 pad 3: /!!! -> /PB14
- Q17 pad 1: GND -> Net-(Q17-Pad1)
- Q17 pad 2: unconnected-(Q17-Pad2) -> GND
- Q17 pad 3: Net-(Q17-Pad3) -> Net-(D15-Pad3)
- Q4 pad 2: GND -> unconnected-(Q4-Pad2)
- Q4 pad 3: /OD 2A3/IN -> Net-(Q4-Pad3)
- Q5 pad 1: /OD 2A3/IN -> Net-(Q5-Pad1)
- Q5 pad 2: unconnected-(Q5-Pad2) -> GND
- Q6 pad 3: Net-(Q6-Pad3) -> Net-(Q4-Pad1)
- R144 pad 1: /!!! -> /PB14
- R145 pad 1: /!!! -> /PB14
- R152 pad 2: Net-(C50-Pad1) -> Net-(C25-Pad1)
- R153 pad 1: Net-(C50-Pad1) -> Net-(C25-Pad1)
- R153 pad 2: Net-(Q17-Pad3) -> Net-(D29-Pad3)
- R154 pad 1: Net-(C50-Pad1) -> Net-(C25-Pad1)
- R154 pad 2: Net-(R154-Pad2) -> +5V
- R155 pad 2: Net-(R154-Pad2) -> +5V
- R156 pad 2: Net-(R154-Pad2) -> +5V
- R157 pad 1: Net-(D15-Pad1) -> Net-(D23-Pad1)
- R157 pad 2: Net-(R154-Pad2) -> +5V
- R158 pad 1: GND -> Net-(R158-Pad1)
- R158 pad 2: /!!! -> +5V
- R161 pad 1: Net-(Q18-Pad1) -> Net-(R161-Pad1)
- R161 pad 2: Net-(R161-Pad2) -> GND
- R162 pad 1: Net-(R161-Pad2) -> Net-(R161-Pad1)
- R163 pad 1: Net-(R161-Pad2) -> Net-(R163-Pad1)
- R164 pad 1: Net-(R161-Pad2) -> /IAT
- R164 pad 2: GND -> +3.3V
- R199 pad 1: /MCU/PB1 -> Net-(R18-Pad2)
- R200 pad 1: /MCU/PB1 -> Net-(R18-Pad2)
- R200 pad 2: unconnected-(R200-Pad2) -> GND
- R35 pad 1: /OD 2A3/IN -> /INJ_7
- R35 pad 2: +5V -> Net-(Q4-Pad3)
- R36 pad 1: /OD 2A3/IN -> Net-(Q4-Pad1)
- R36 pad 2: Net-(R36-Pad2) -> Net-(Q5-Pad3)
- R37 pad 1: Net-(Q4-Pad1) -> Net-(Q5-Pad1)
- R37 pad 2: Net-(R37-Pad2) -> /PD0
- R38 pad 1: Net-(R37-Pad2) -> Net-(Q4-Pad1)
- R38 pad 2: GND -> Net-(Q4-Pad3)
- R39 pad 1: Net-(R37-Pad2) -> Net-(Q4-Pad1)
- R39 pad 2: GND -> Net-(R39-Pad2)
- R40 pad 1: Net-(R37-Pad2) -> Net-(Q6-Pad1)
- R40 pad 2: GND -> Net-(R161-Pad1)
- R41 pad 1: /PD1 -> Net-(R161-Pad1)
- R41 pad 2: /INJ_7 -> GND
- R42 pad 1: GND -> Net-(R161-Pad1)
- R42 pad 2: /PD1 -> GND
- R43 pad 1: unconnected-(R43-Pad1) -> Net-(R161-Pad1)
- R43 pad 2: Net-(Q5-Pad3) -> GND
- R44 pad 1: /OD 2A3/IN -> /PD1
- R44 pad 2: Net-(Q6-Pad3) -> /INJ_7
- R45 pad 1: Net-(Q6-Pad1) -> GND
- R45 pad 2: /PD0 -> /PD1
- R46 pad 1: unconnected-(R46-Pad1) -> +5V
- R57 pad 1: Net-(Q8-Pad1) -> Net-(R57-Pad1)
- R57 pad 2: Net-(R57-Pad2) -> GND
- R58 pad 1: Net-(R57-Pad2) -> /PA15
- R58 pad 2: GND -> /INJ_6/AFR_2_Heater
- R59 pad 1: Net-(R57-Pad2) -> GND
- R59 pad 2: GND -> /PA15
- R60 pad 1: Net-(R57-Pad2) -> +5V
- R60 pad 2: GND -> /PD15
- R61 pad 1: /PA15 -> /PD15
- R61 pad 2: /INJ_6/AFR_2_Heater -> Net-(R61-Pad2)
- R62 pad 1: GND -> /PD13
- R62 pad 2: /PA15 -> Net-(VT23-Pad1)
- R68 pad 1: /IGN driver2/FB -> GND
- R68 pad 2: Net-(C45-Pad1) -> Net-(VT23-Pad1)
- R69 pad 1: /IGN_3 -> /PD12
- R69 pad 2: Net-(R69-Pad2) -> Net-(VT7-Pad1)
- R70 pad 1: Net-(R69-Pad2) -> GND
- R70 pad 2: Net-(D9-Pad2) -> Net-(VT7-Pad1)
- R71 pad 1: Net-(D9-Pad2) -> /PD14
- R71 pad 2: Net-(C45-Pad1) -> Net-(R71-Pad2)
- R72 pad 1: Net-(C45-Pad1) -> /MCU/PB15
- R73 pad 1: /IGN driver3/FB -> Net-(R73-Pad1)
- R73 pad 2: Net-(C48-Pad1) -> GND
- R74 pad 1: /IGN_4 -> +5V
- R74 pad 2: Net-(R74-Pad2) -> Net-(R73-Pad1)
- R75 pad 1: Net-(R74-Pad2) -> Net-(R75-Pad1)
- R75 pad 2: Net-(D10-Pad2) -> GND
- R76 pad 1: Net-(D10-Pad2) -> /AFR_1
- R76 pad 2: Net-(C48-Pad1) -> /PA7
- R77 pad 1: Net-(C48-Pad1) -> Net-(R75-Pad1)
- R77 pad 2: GND -> /AFR_1
- R80 pad 2: /PD15 -> Net-(R75-Pad1)
- R82 pad 1: GND -> Net-(R73-Pad1)
- R82 pad 2: /IGN driver/IN -> /AFR_2
- R83 pad 1: GND -> /AFR_2
- R83 pad 2: /IGN driver1/IN -> /PC5
- R86 pad 1: /PD13 -> /IAT
- R86 pad 2: /IGN driver/IN -> GND
- R87 pad 1: /PD12 -> /CLT
- R87 pad 2: /IGN driver1/IN -> GND
- R88 pad 1: /PD15 -> /IAT
- R88 pad 2: /IGN driver2/IN -> +3.3V
- R89 pad 1: /PD14 -> +3.3V
- R89 pad 2: /IGN driver3/IN -> /CLT
- U2 pad 26: /MCU/PA3 -> /PA3
- U2 pad 31: /MCU/PA6 -> /PA6
- U2 pad 32: /MCU/PA7 -> /PA7
- U2 pad 33: /MCU/PC4 -> /PC4
- U2 pad 34: /MCU/PC5 -> /PC5
- U2 pad 90: /MCU/PB4 -> /PB4
- VT18 pad 3: Net-(R161-Pad2) -> Net-(R163-Pad1)
- VT23 pad 1: /IGN driver/IN -> Net-(VT23-Pad1)
- VT4 pad 1: Net-(R36-Pad2) -> Net-(R39-Pad2)
- VT4 pad 3: Net-(R37-Pad2) -> Net-(R161-Pad1)
- VT6 pad 3: Net-(R57-Pad2) -> Net-(R57-Pad1)
- VT7 pad 1: /IGN driver1/IN -> Net-(VT7-Pad1)
- VT8 pad 1: /IGN driver2/IN -> Net-(R61-Pad2)
- VT9 pad 1: /IGN driver3/IN -> Net-(R71-Pad2)
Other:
- board size 189.1 x 227.2 mm -> 86 x 159 mm
- board text removed: "+2 по 100 ОМ"
